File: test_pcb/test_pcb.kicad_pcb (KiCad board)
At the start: 2 copper layers, 77 x 114 mm, 88 parts, among them K0 KEYSW, K1 KEYSW, K10 KEYSW, K12 KEYSW, K13 KEYSW, K14 KEYSW, K15 KEYSW, K16 KEYSW, K17 KEYSW, K18 KEYSW, K2 KEYSW, K20 KEYSW, K21 KEYSW, K22 KEYSW, K3 KEYSW, K4 KEYSW, K5 KEYSW, K6 KEYSW, K7 KEYSW, K8 KEYSW, K9 KEYSW, P1 CONN_01X15, P10 CONN_01X01, P11 CONN_01X01, P12 CONN_01X01, P13 CONN_01X01, P14 CONN_01X01, P15 CONN_01X01, P2 CONN_01X08, P3 CONN_01X06, P4 CONN_01X01, P5 CONN_01X01, P6 CONN_01X01, P7 CONN_01X01, P8 CONN_01X01, P9 CONN_01X01, U1 STP16CP05

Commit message: test groud plane
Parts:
- moved P14 75.5 mm to (136.0, 120.5)
- moved P4 60.1 mm to (99.0, 103.8)
- moved P13 29.4 mm to (87.2, 36.5)
- moved P15 28.1 mm to (135.5, 68.0), turned to 270 degrees
- moved P11 18.1 mm to (81.8, 36.8)
- moved P10 10.7 mm to (55.8, 155.2)
- moved P7 10.7 mm to (52.8, 152.0)
- moved P8 10.7 mm to (52.5, 155.5)
- moved P9 9.91 mm to (74.2, 36.5)
- moved P12 7.95 mm to (67.0, 36.5)
- moved P5 7.12 mm to (126.0, 159.5)
- moved P6 7.12 mm to (128.5, 159.5)
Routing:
- net c1: track 160.0 -> 165.2 mm
- net green1: track 173.1 -> 176.7 mm
- net c0: track 163.7 -> 167.3 mm
- net green0: track 146.1 -> 149.6 mm
- net red1: track 158.3 -> 161.2 mm
- net c3: track 144.3 -> 141.6 mm, vias 0 -> 2
- net blue0: track 153.7 -> 155.0 mm
- net red0: track 147.0 -> 148.0 mm
- net r0: track 59.2 -> 60.1 mm
- net SDI: track 8.97 -> 9.89 mm
- net blue2: track 179.8 -> 180.6 mm, vias 5 -> 6
- net r1: track 67.2 -> 67.9 mm
- net c2: track 129.7 -> 130.3 mm
- net CLK: track 9.30 -> 9.81 mm
- net +3V3: track 7.45 -> 6.94 mm

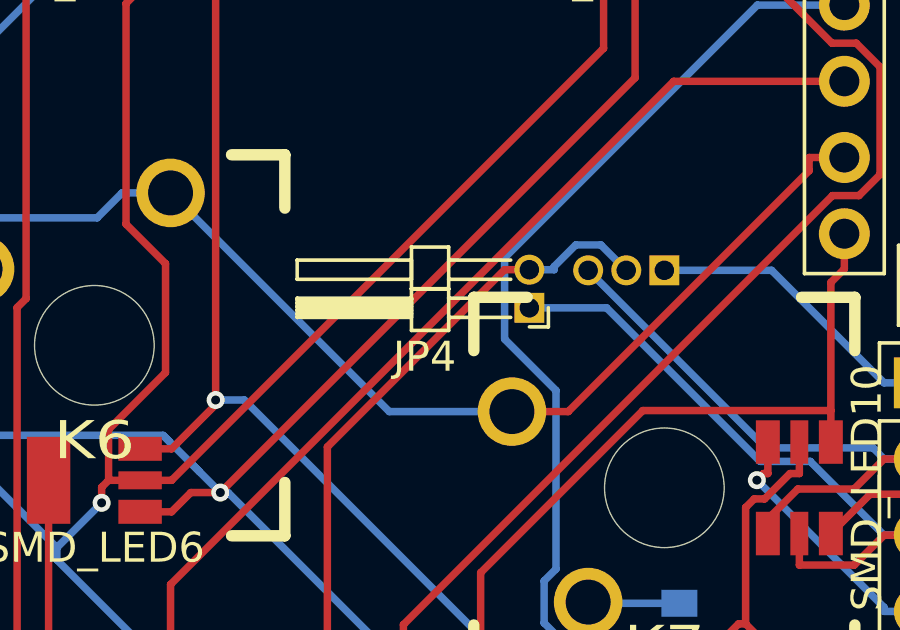
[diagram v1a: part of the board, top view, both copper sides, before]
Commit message: added flipped angled 01x02 header footprint
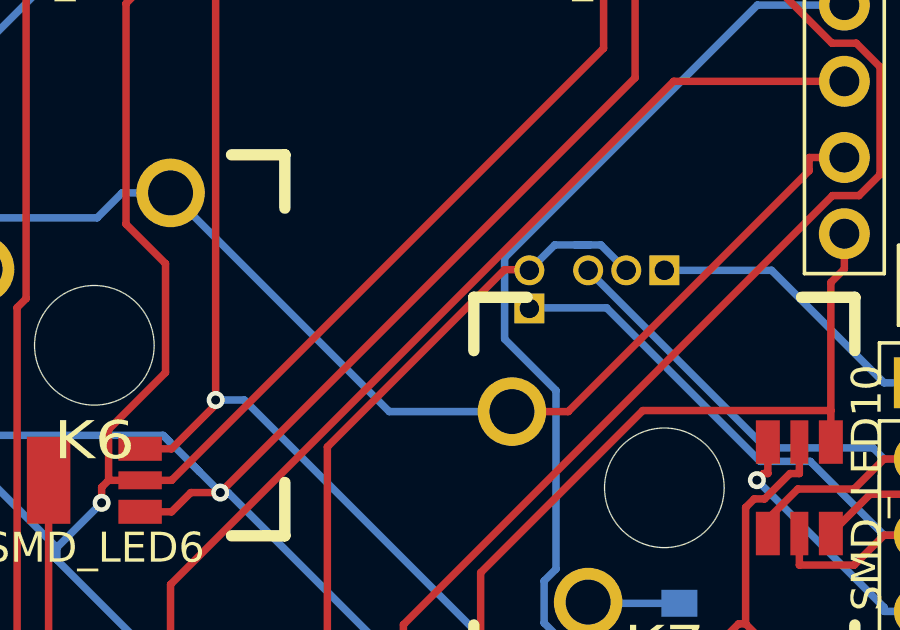
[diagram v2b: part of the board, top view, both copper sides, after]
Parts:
- JP4: footprint Pin_Headers:Pin_Header_Angled_1x02_Pitch1.27mm -> cherry_rgb:Pin_Header_Angled_1x02_Pitch1.27mm_flipped; moved to B.Cu
- moved JP4 1.25 mm to (122.5, 67.5)

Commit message: test groundplanes
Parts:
- P10, P11, P12, P13, P14, P15, P4, P5, P6, P7, P8, P9: footprint Socket_Strips:Socket_Strip_Straight_1x01_Pitch1.27mm -> cherry_rgb:VIA127
- moved P12 133.0 mm to (99.0, 165.6), turned to 0 degrees
- moved P9 131.4 mm to (99.0, 165.6), turned to 0 degrees
- moved P11 130.0 mm to (99.0, 165.6), turned to 0 degrees
- moved P13 129.6 mm to (99.0, 165.6), turned to 0 degrees
- moved P15 104.2 mm to (99.0, 165.6), turned to 0 degrees
- moved P5 94.7 mm to (139.2, 65.8), turned to 0 degrees
- moved P14 58.3 mm to (99.0, 165.6), turned to 0 degrees
- moved P7 48.2 mm to (99.0, 165.6), turned to 0 degrees
- moved P8 47.6 mm to (99.0, 165.6), turned to 0 degrees
- moved P10 44.5 mm to (99.0, 165.6), turned to 0 degrees
- moved P6 30.1 mm to (99.0, 165.6), turned to 0 degrees
- moved P4 16.0 mm to (115.0, 102.8), turned to 0 degrees
- moved JP3 6.25 mm to (117.8, 97.2)
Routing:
- net c3: track 141.6 -> 134.9 mm, vias 2 -> 4
- net red2: track 191.4 -> 197.7 mm
- net a3: track 73.4 -> 67.6 mm
- net a2: track 100.3 -> 103.6 mm
- net r5: track 59.8 -> 62.7 mm
- net a3-17-0: track 26.7 -> 29.3 mm
- net Net-(JP1-Pad2): track 34.0 -> 31.3 mm
- net Net-(JP3-Pad1): track 39.2 -> 37.3 mm
- net r0: track 60.1 -> 62.0 mm
- net green2: track 171.5 -> 173.4 mm, vias 1 -> 3
- net a5: track 121.3 -> 123.0 mm
- net green0: track 149.6 -> 151.3 mm
- net blue1: track 154.1 -> 152.6 mm, vias 6 -> 7
- net r3: track 81.2 -> 82.4 mm
- net a6: track 93.3 -> 92.3 mm
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
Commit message: test more gp
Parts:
- moved P7 68.2 mm to (85.2, 98.8)
- moved P6 66.8 mm to (97.2, 98.8)
- moved P5 47.6 mm to (105.5, 99.2)
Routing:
- net r3: track 82.4 -> 82.9 mm
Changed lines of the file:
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@@
   (general
     (links 192)
-    (no_connects 4)
+    (no_connects 3)
     (area 60.424999 41.424999 137.575001 155.575001)
     (thickness 1.6)
     (drawings 6)
-    (tracks 1068)
+    (tracks 1071)
     (zones 0)
     (modules 88)
@@
   )
   (module cherry_rgb:VIA127 (layer F.Cu)
-    (at 139.25 65.75)
+    (at 105.5 99.25)
     (fp_text reference P5 (at 0 2.25) (layer F.SilkS) hide
       (effects (font (size 1 1) (thickness 0.15)))
@@
   )
   (module cherry_rgb:VIA127 (layer F.Cu)
-    (at 99 165.575001)
+    (at 97.25 98.75)
     (fp_text reference P6 (at 0 2.25) (layer F.SilkS) hide
       (effects (font (size 1 1) (thickness 0.15)))
@@
   )
   (module cherry_rgb:VIA127 (layer F.Cu)
-    (at 99 165.575001)
+    (at 85.25 98.75)
     (fp_text reference P7 (at 0 2.25) (layer F.SilkS) hide
       (effects (font (size 1 1) (thickness 0.15)))
@@
   (segment (start 109.6327 84.8273) (end 92.4473 84.8273) (width 0.25) (layer B.Cu) (net 25))
   (segment (start 110.54 83.92) (end 109.6327 84.8273) (width 0.25) (layer B.Cu) (net 25))
-  (segment (start 106.62 99) (end 110.54 102.92) (width 0.25) (layer B.Cu) (net 26))
-  (segment (start 91.54 100.0748) (end 92.6148 99) (width 0.25) (layer B.Cu) (net 26))
-  (segment (start 106.62 99) (end 92.6148 99) (width 0.25) (layer B.Cu) (net 26))
+  (segment (start 102.5 99) (end 99.75 99) (width 0.25) (layer B.Cu) (net 26))
+  (segment (start 110.54 102.92) (end 106.42 102.92) (width 0.25) (layer B.Cu) (net 26))
+  (segment (start 106.42 102.92) (end 102.5 99) (width 0.25) (layer B.Cu) (net 26))
+  (segment (start 91 100.0746) (end 75.3854 100.0746) (width 0.25) (layer B.Cu) (net 26))
+  (segment (start 91.5398 100.0746) (end 91 100.0746) (width 0.25) (layer B.Cu) (net 26))
+  (segment (start 91 100.0746) (end 98.6754 100.0746) (width 0.25) (layer B.Cu) (net 26))
+  (segment (start 98.6754 100.0746) (end 99.75 99) (width 0.25) (layer B.Cu) (net 26))
   (segment (start 118.25 104.75) (end 118.25 106.87) (width 0.25) (layer B.Cu) (net 26))
   (segment (start 118.25 104) (end 118.25 104.75) (width 0.25) (layer B.Cu) (net 26))
@@
   (segment (start 91.54 102.92) (end 91.54 100.0748) (width 0.25) (layer B.Cu) (net 26))
   (segment (start 75.3854 100.0746) (end 72.54 102.92) (width 0.25) (layer B.Cu) (net 26))
-  (segment (start 91.5398 100.0746) (end 75.3854 100.0746) (width 0.25) (layer B.Cu) (net 26))
   (segment (start 91.54 100.0748) (end 91.5398 100.0746) (width 0.25) (layer B.Cu) (net 26))
   (via (at 103.6111 121.9512) (size 0.6) (layers F.Cu B.Cu) (net 27))
@@
   (segment (start 109.525 74.5) (end 110.5753 74.5) (width 0.25) (layer F.Cu) (net 29))
   (segment (start 126.025 55.5) (end 124.9747 55.5) (width 0.25) (layer F.Cu) (net 29))
+  (segment (start 110.5464 91.7246) (end 108.5595 91.7246) (width 0.25) (layer F.Cu) (net 30))
+  (segment (start 108.5595 91.7246) (end 107.5474 92.7367) (width 0.25) (layer F.Cu) (net 30))
+  (segment (start 107.5474 92.7367) (end 107.5474 105.1283) (width 0.25) (layer F.Cu) (net 30))
+  (segment (start 107.5474 105.1283) (end 105.6757 107) (width 0.25) (layer F.Cu) (net 30))
+  (segment (start 105.6757 107) (end 105.6757 108.9795) (width 0.25) (layer F.Cu) (net 30))
+  (segment (start 108.4747 111.7785) (end 108.4747 112.5) (width 0.25) (layer F.Cu) (net 30))
+  (segment (start 105.6757 108.9795) (end 108.4747 111.7785) (width 0.25) (layer F.Cu) (net 30))
+  (segment (start 108.4747 112.5) (end 109.525 112.5) (width 0.25) (layer F.Cu) (net 30))
   (segment (start 114.5 91) (end 111.1601 91) (width 0.25) (layer B.Cu) (net 30))
   (segment (start 111.1601 91) (end 110.5464 91.6137) (width 0.25) (layer B.Cu) (net 30))
@@
   (via (at 120.9929 87.7667) (size 0.6) (layers F.Cu B.Cu) (net 30))
   (via (at 76.9333 93.5351) (size 0.6) (layers F.Cu B.Cu) (net 30))
-  (segment (start 109.525 112.5) (end 108.4747 112.5) (width 0.25) (layer F.Cu) (net 30))
   (segment (start 109.525 93.5) (end 110.5753 93.5) (width 0.25) (layer F.Cu) (net 30))
   (segment (start 110.5464 91.6137) (end 110.5464 91.7246) (width 0.25) (layer F.Cu) (net 30))
@@
   (segment (start 129.4744 79.2852) (end 120.9929 87.7667) (width 0.25) (layer F.Cu) (net 30))
   (segment (start 129.7088 79.2852) (end 129.4744 79.2852) (width 0.25) (layer F.Cu) (net 30))
-  (segment (start 108.5595 91.7246) (end 110.5464 91.7246) (width 0.25) (layer F.Cu) (net 30))
-  (segment (start 107.5474 92.7367) (end 108.5595 91.7246) (width 0.25) (layer F.Cu) (net 30))
-  (segment (start 107.5474 96.399) (end 107.5474 92.7367) (width 0.25) (layer F.Cu) (net 30))
-  (segment (start 105.6757 98.2707) (end 107.5474 96.399) (width 0.25) (layer F.Cu) (net 30))
-  (segment (start 105.6757 108.9795) (end 105.6757 98.2707) (width 0.25) (layer F.Cu) (net 30))
-  (segment (start 108.4747 111.7785) (end 105.6757 108.9795) (width 0.25) (layer F.Cu) (net 30))
-  (segment (start 108.4747 112.5) (end 108.4747 111.7785) (width 0.25) (layer F.Cu) (net 30))
   (segment (start 90.525 93.5) (end 89.4747 93.5) (width 0.25) (layer F.Cu) (net 30))
   (segment (start 90.525 112.5) (end 91.5753 112.5) (width 0.25) (layer F.Cu) (net 30))
@@
   (segment (start 126.3553 123.5848) (end 126.3566 123.5861) (width 0.25) (layer F.Cu) (net 37))
   (segment (start 126.3553 123.5848) (end 124.4647 125.4754) (width 0.25) (layer F.Cu) (net 37))
-  (segment (start 126.325 92.1) (end 126.325 92.9753) (width 0.25) (layer B.Cu) (net 38))
-  (segment (start 126.325 92.9753) (end 118.6775 100.6228) (width 0.25) (layer B.Cu) (net 38))
-  (segment (start 74.8053 97.5) (end 73 95.6947) (width 0.25) (layer B.Cu) (net 38))
-  (segment (start 118.6775 100.6228) (end 110.9169 100.6228) (width 0.25) (layer B.Cu) (net 38))
-  (segment (start 110.9169 100.6228) (end 107.7941 97.5) (width 0.25) (layer B.Cu) (net 38))
-  (segment (start 107.7941 97.5) (end 74.8053 97.5) (width 0.25) (layer B.Cu) (net 38))
-  (segment (start 73 95.6947) (end 73 91.75) (width 0.25) (layer B.Cu) (net 38))
+  (segment (start 73 91.75) (end 73 95.6947) (width 0.25) (layer B.Cu) (net 38))
+  (segment (start 126.325 92.9753) (end 126.325 92.1) (width 0.25) (layer B.Cu) (net 38))
+  (segment (start 73 95.6947) (end 74.5553 97.25) (width 0.25) (layer B.Cu) (net 38))
+  (segment (start 74.5553 97.25) (end 107.5441 97.25) (width 0.25) (layer B.Cu) (net 38))
+  (segment (start 107.5441 97.25) (end 110.9169 100.6228) (width 0.25) (layer B.Cu) (net 38))
+  (segment (start 110.9169 100.6228) (end 118.6775 100.6228) (width 0.25) (layer B.Cu) (net 38))
+  (segment (start 118.6775 100.6228) (end 126.325 92.9753) (width 0.25) (layer B.Cu) (net 38))
   (segment (start 68.5099 91.6976) (end 72.9476 91.6976) (width 0.25) (layer F.Cu) (net 38))
   (segment (start 72.9476 91.6976) (end 73 91.75) (width 0.25) (layer F.Cu) (net 38))

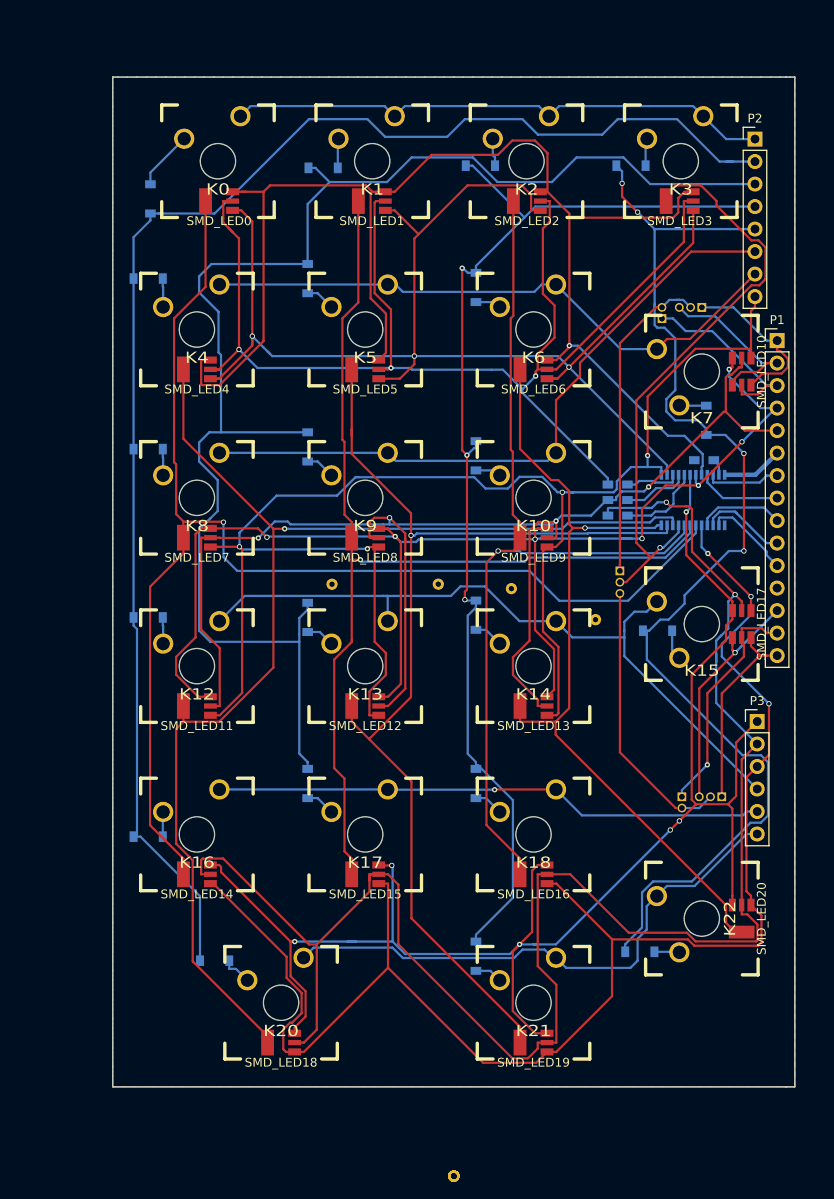
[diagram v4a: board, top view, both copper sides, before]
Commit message: test groundplane loop eliminiation
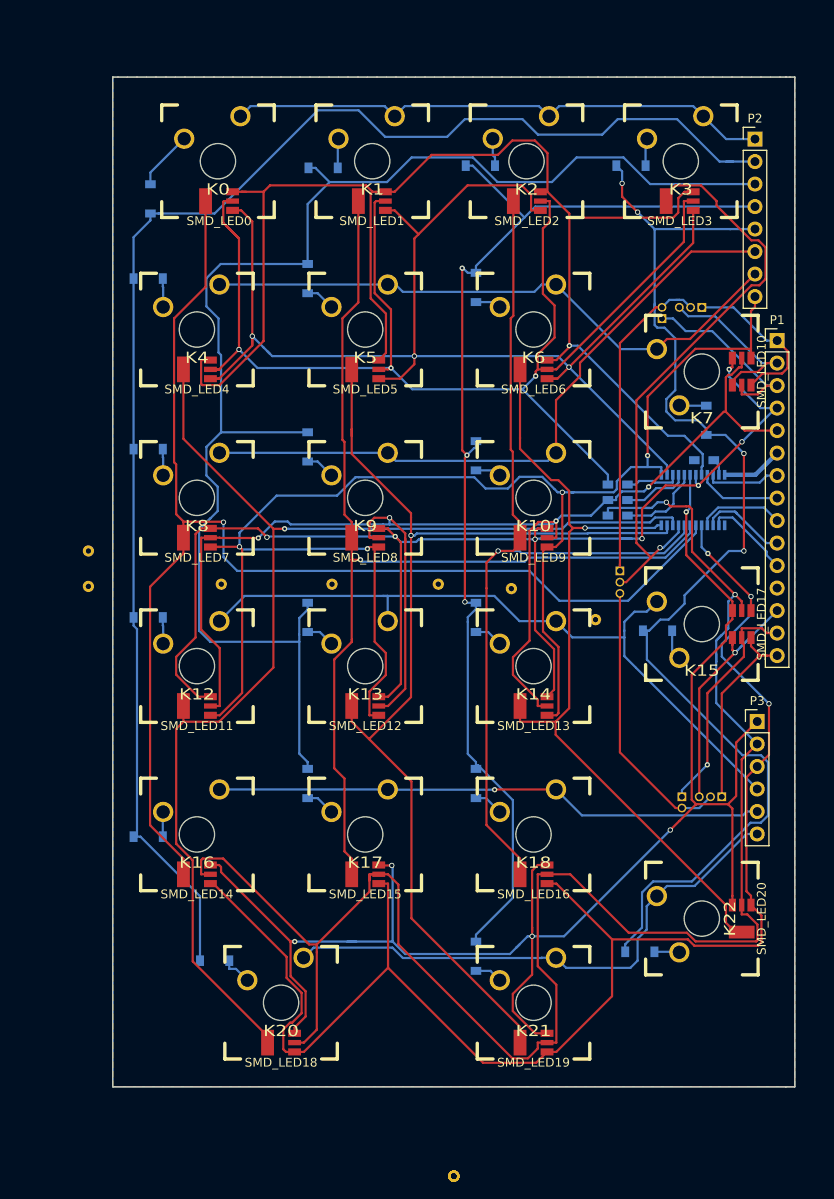
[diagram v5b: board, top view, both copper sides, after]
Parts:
- P10: moved to B.Cu
- moved P10 81.7 mm to (57.8, 95.0)
- moved P9 78.3 mm to (57.8, 99.0)
- moved P8 71.8 mm to (72.8, 98.8)
- moved D14 0.25 mm to (101.5, 102.5)
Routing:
- net c1: track 165.2 -> 162.4 mm
- net red0: track 148.0 -> 150.1 mm
- net r3: track 82.9 -> 82.0 mm
- net c0: track 167.4 -> 168.2 mm
- net r5: track 62.7 -> 61.9 mm
- net blue2: track 180.5 -> 181.1 mm, vias 6 -> 5

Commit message: test groundplane loop eliminiation, they are sneeky
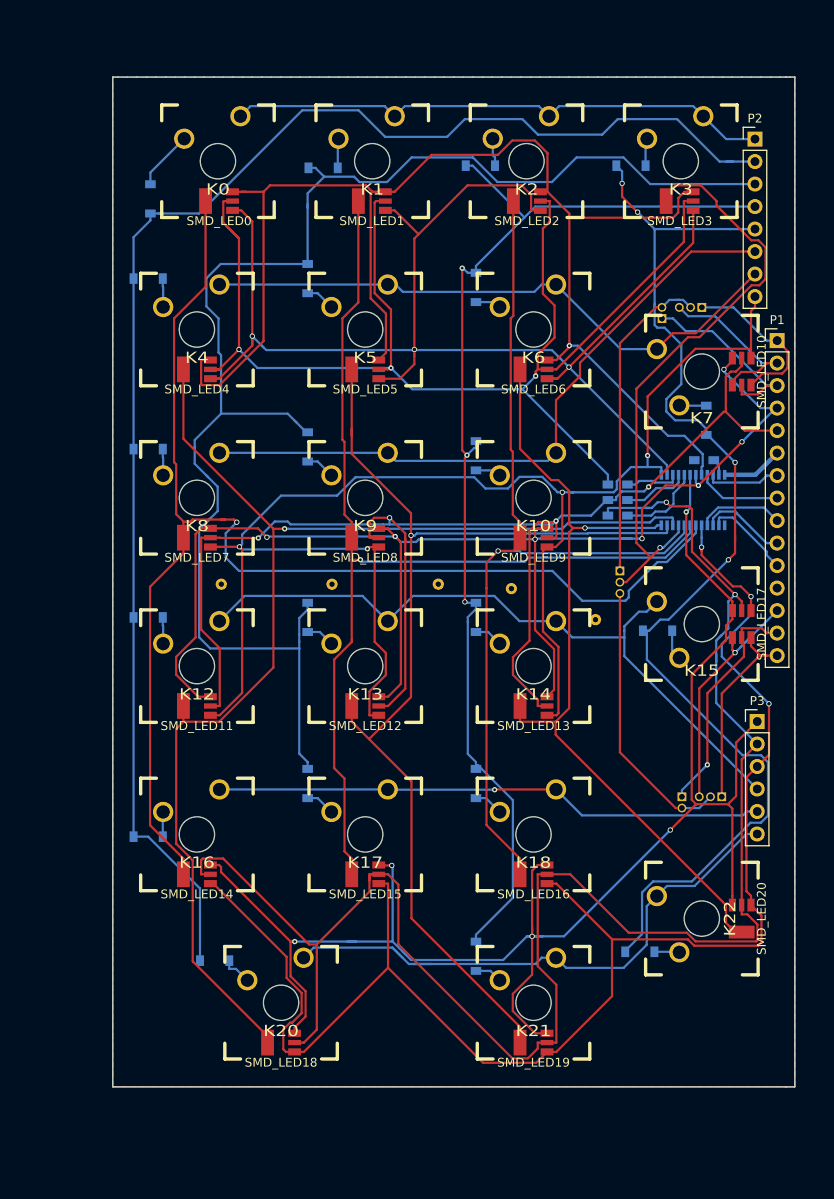
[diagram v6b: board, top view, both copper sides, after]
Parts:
- removed P10, P11, P12, P13, P14, P15, P9: CONN_01X01, cherry_rgb:VIA127
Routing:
- net c1: track 162.4 -> 167.0 mm
- net r5: track 61.9 -> 65.9 mm
- net a0: track 148.9 -> 151.8 mm
- net blue2: track 181.1 -> 183.2 mm
- net c3: track 134.9 -> 133.2 mm
- net r3: track 82.0 -> 80.7 mm
- net green2: track 173.4 -> 174.4 mm
- net a3: track 67.6 -> 68.4 mm
- net blue1: track 152.6 -> 153.3 mm

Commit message: test ground planes nearing completion
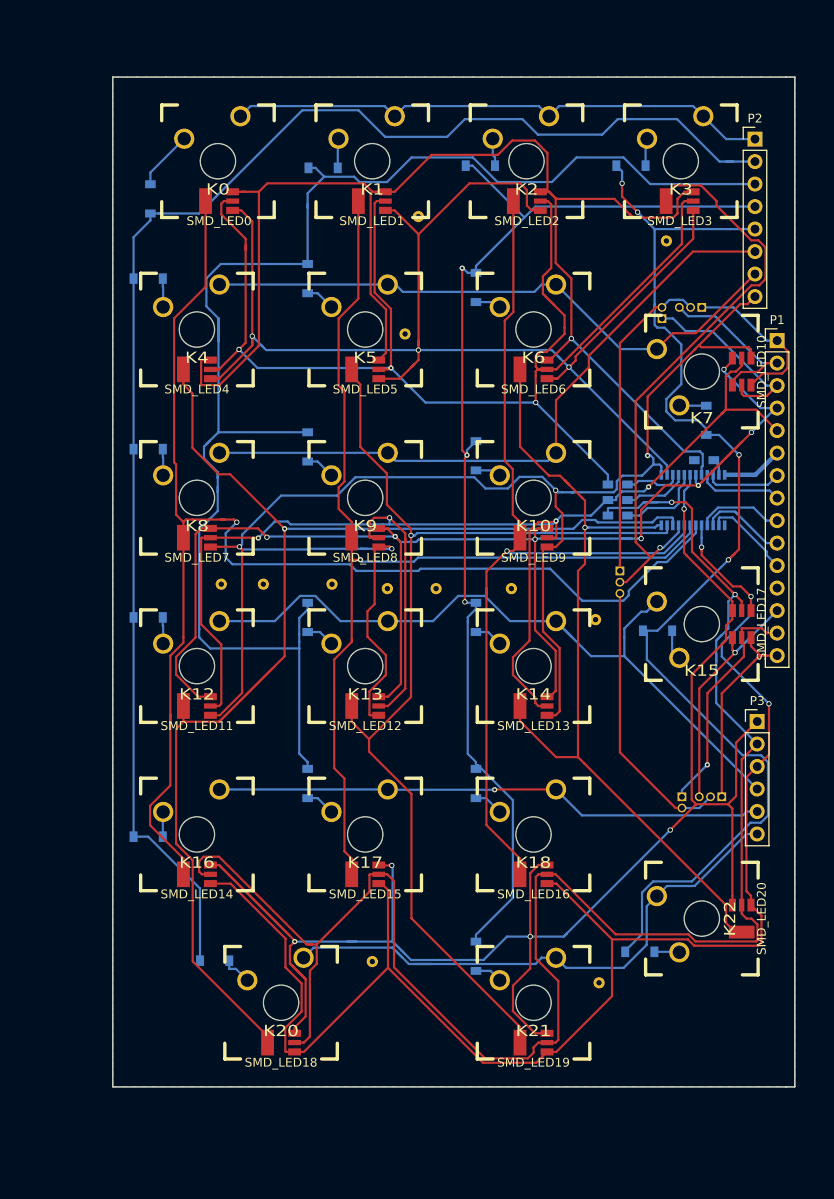
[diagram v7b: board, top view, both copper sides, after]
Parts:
- added P10: CONN_01X01, cherry_rgb:VIA127, F.Cu at (115.4, 143.8)
- added P11: CONN_01X01, cherry_rgb:VIA127, F.Cu at (89.8, 141.3)
- added P12: CONN_01X01, cherry_rgb:VIA127, F.Cu at (77.5, 98.8)
- added P13: CONN_01X01, cherry_rgb:VIA127, F.Cu at (93.5, 70.5)
- added P14: CONN_01X01, cherry_rgb:VIA127, F.Cu at (95.0, 57.2)
- added P15: CONN_01X01, cherry_rgb:VIA127, F.Cu at (91.5, 99.2)
- added P9: CONN_01X01, cherry_rgb:VIA127, F.Cu at (123.0, 60.0)
- moved P6 0.56 mm to (97.0, 99.2)
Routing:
- net blue2: track 183.2 -> 197.1 mm
- net a4: track 139.6 -> 149.0 mm
- net green1: track 177.1 -> 185.7 mm
- net blue1: track 153.3 -> 160.6 mm
- net blue0: track 155.1 -> 159.6 mm
- net red0: track 150.1 -> 154.6 mm
- net r3: track 80.7 -> 84.0 mm
- net a6: track 92.3 -> 95.1 mm
- net red2: track 197.7 -> 199.8 mm
- net c1: track 167.0 -> 169.0 mm
- net c3: track 133.2 -> 134.8 mm
- net green0: track 150.9 -> 152.0 mm
- net a0: track 151.8 -> 152.9 mm
- net a1: track 119.3 -> 120.2 mm
- net a5: track 123.0 -> 122.2 mm
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
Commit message: test gp tweaks
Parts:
- moved P4 0.50 mm to (115.5, 102.8)
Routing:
- net a3-17-2: track 22.1 -> 29.9 mm
- net green1: track 185.7 -> 186.6 mm
- net blue0: track 159.6 -> 158.8 mm
- net a3: track 67.7 -> 68.4 mm
